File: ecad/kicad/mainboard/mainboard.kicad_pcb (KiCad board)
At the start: 2 copper layers, 99.1 x 81.3 mm, 34 parts, among them IC1 74HC86, J1 SENSORS, J2 CONN_06SILK_FEMALE_PTH, J3 CONN_06SILK_FEMALE_PTH, J4 POWER, J5 SERIAL, M1 Left Motor, M2 Right Motor, U1 Arduino_Nano, U2 TB6612FNG-Module

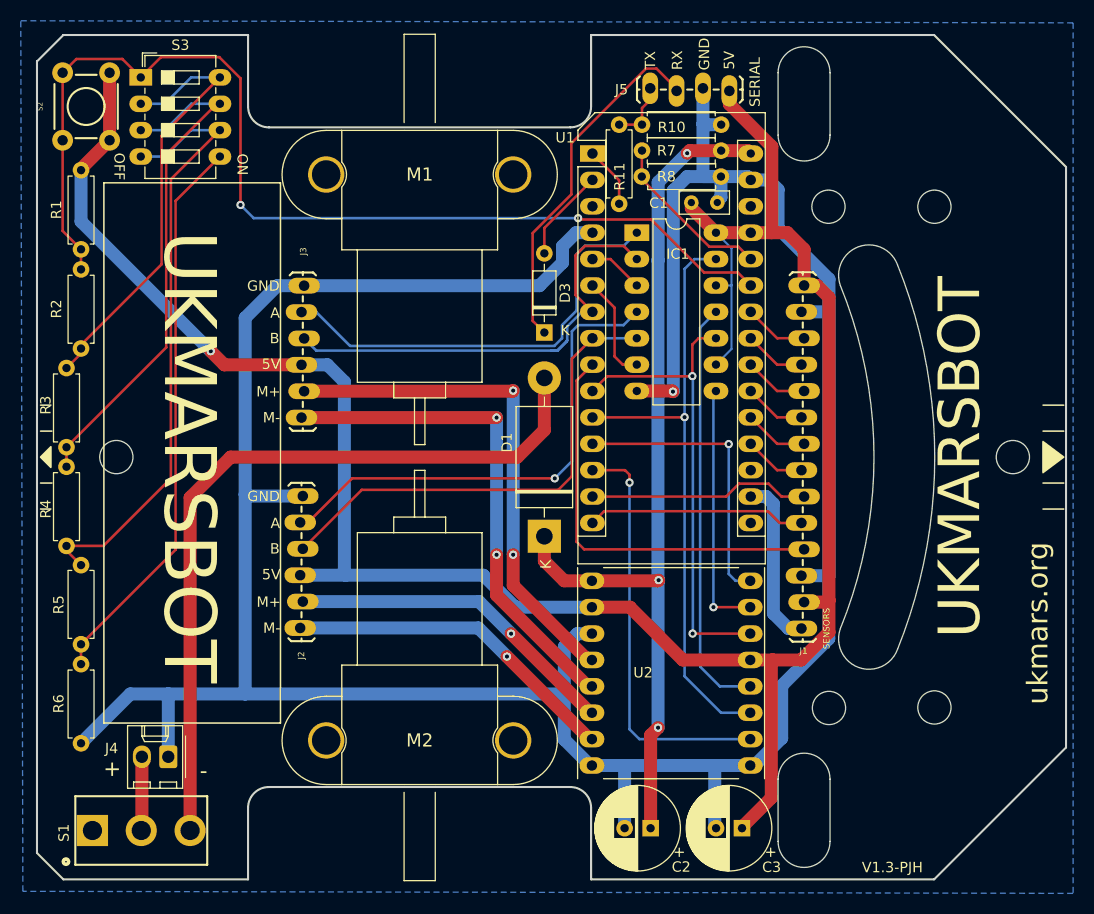
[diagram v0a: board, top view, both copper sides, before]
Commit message: re-route kicad mainboard with bigger pads
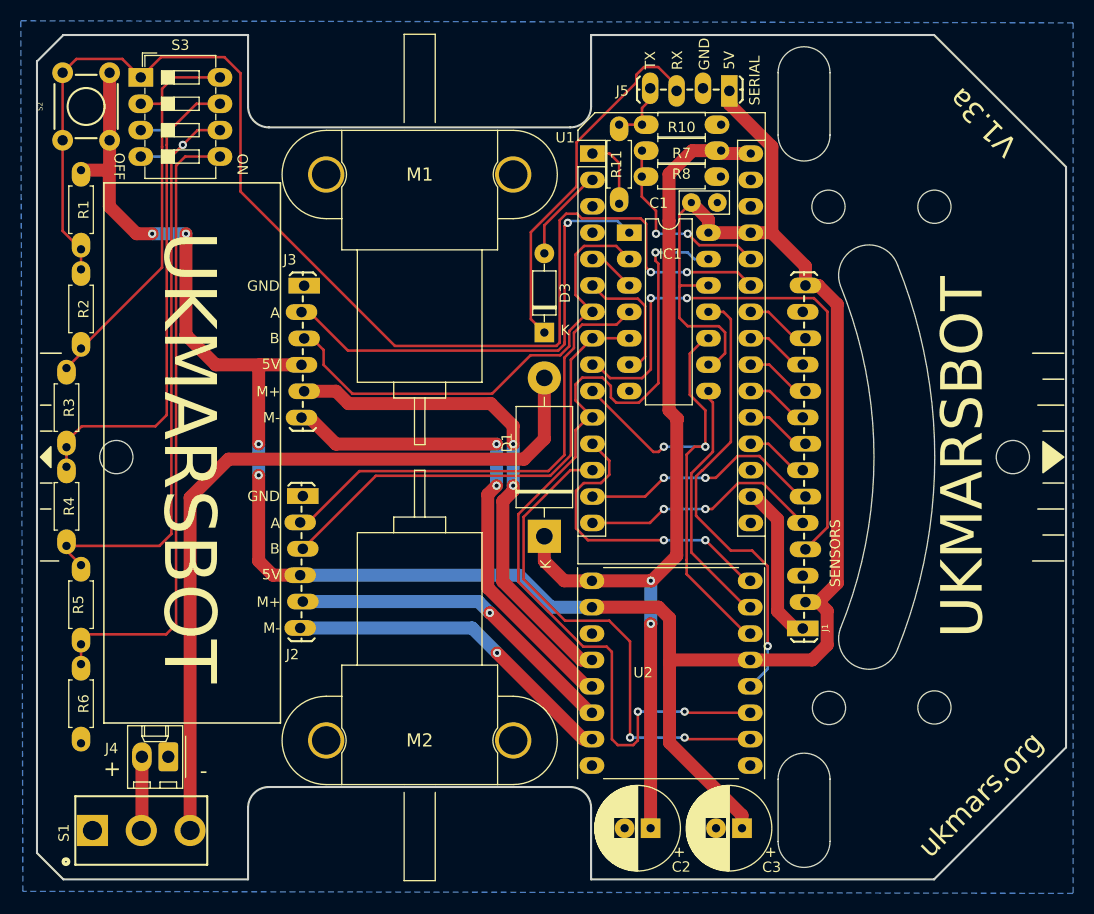
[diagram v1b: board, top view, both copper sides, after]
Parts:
- R1, R10, R11, R2, R3, R4, R5, R6, R7, R8: footprint ukmarsbot:R_Axial_DIN0207_L6.3mm_D2.5mm_P7.62mm_Horizontal -> ukmarsbot:R_Axial_DIN0207_L6.3mm_D2.5mm_P7.62mm_BIGPAD
- moved IC1 0.73 mm to (125.2, 83.4)
- turned J1 to 180 degrees
- turned J2 to 0 degrees
- turned J3 to 0 degrees
- turned J5 to -90 degrees
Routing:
- net GND: track 291.8 -> 0.00 mm, vias 1 -> 0
- net /RIGHT_DIR: track 59.3 -> 88.0 mm, vias 1 -> 3
- net /FUNCTION_SELECT: track 103.9 -> 123.7 mm
- net 5V: track 222.9 -> 238.5 mm, vias 1 -> 4
- net /USER_IO: track 39.9 -> 54.3 mm, vias 0 -> 2
- net /RIGHT_PWM: track 40.2 -> 48.1 mm, vias 1 -> 2
- net Net-(R5-Pad2): track 54.4 -> 60.2 mm
- net Net-(R2-Pad1): track 42.8 -> 38.3 mm
- net //RIGHT_DIR: track 40.4 -> 44.0 mm, vias 0 -> 1
- net /LEFT_A: track 42.1 -> 44.6 mm, vias 0 -> 1
- net /BATTERY_VOLTS: track 16.2 -> 18.7 mm, vias 0 -> 2
- net /EMITTER_B: track 21.1 -> 23.4 mm, vias 0 -> 2
- net /3V3: track 16.3 -> 14.3 mm
- net /RIGHT_B: track 47.2 -> 45.2 mm
- net /EMITTER_A: track 21.4 -> 23.2 mm, vias 0 -> 2
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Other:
- board text added: "V1.3a"
